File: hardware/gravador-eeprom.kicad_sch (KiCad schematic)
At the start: 21 parts, among them J1 Analog, J2 Digital, U1 74HC595, U2 74HC595, U4 28C256

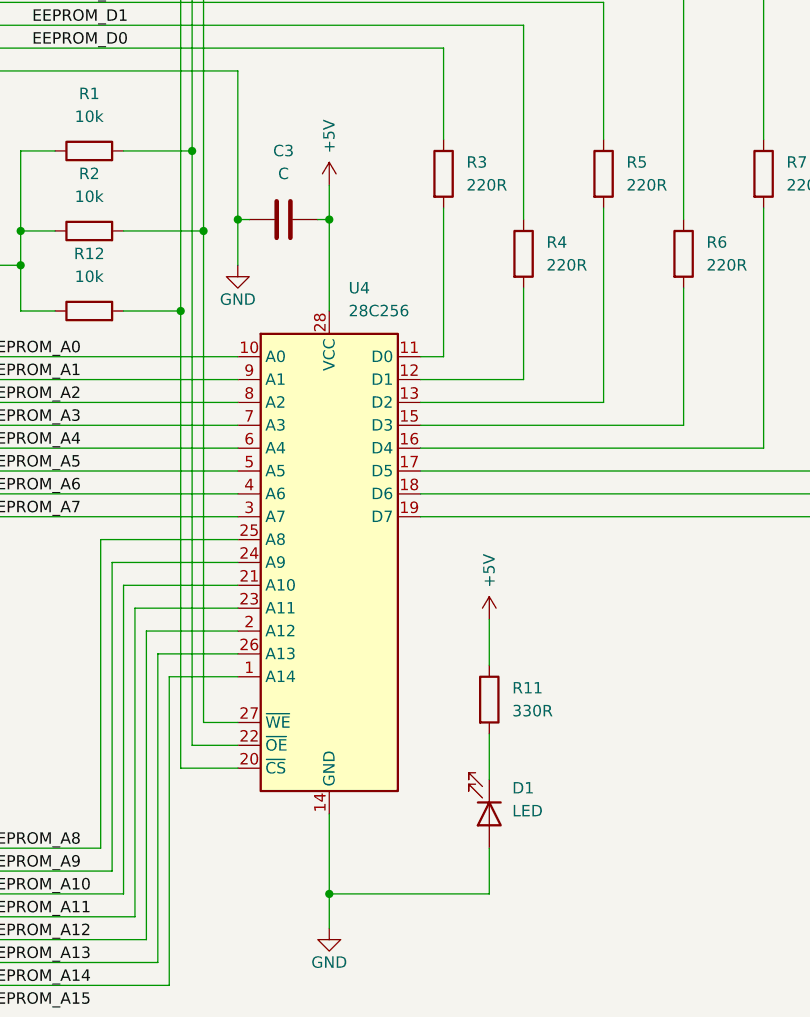
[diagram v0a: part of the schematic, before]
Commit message: Etapa 1: correções no esquema do hardware
- D1 (LED de alimentação) estava invertido: anodo no GND e catodo via
  R11 ao +5V, nunca acenderia. Símbolo girado 180°.
- C3 sem valor definido: agora 10uF (capacitor de reserva do soquete).
- PDF do esquema regenerado.

Co-Authored-By: Claude Opus 5.5 <noreply@anthropic.com>
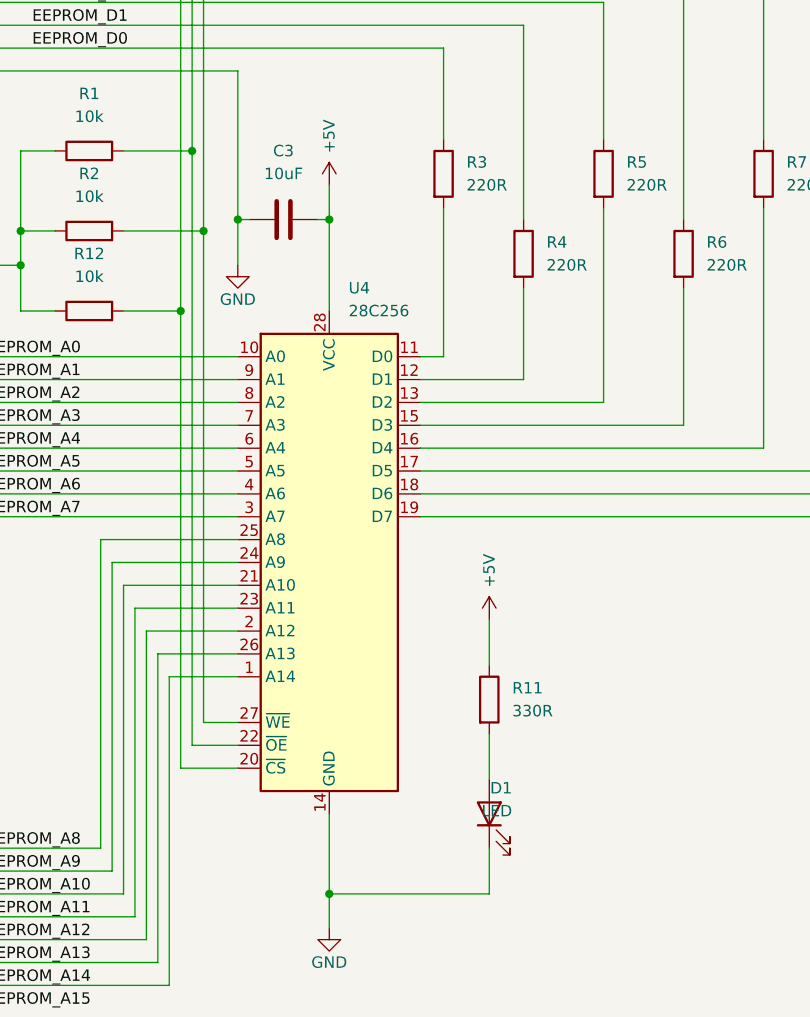
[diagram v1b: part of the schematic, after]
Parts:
- C3: value C -> 10uF
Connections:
- net GND: now also D1.1 (K); no longer D1.2 (A)
- net at R11.2: now also D1.2 (A); no longer D1.1 (K)
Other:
- moved on the sheet: D1
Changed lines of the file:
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@@
 	(symbol
 		(lib_id "Device:LED")
-		(at 162.56 137.16 270)
+		(at 162.56 137.16 90)
 		(unit 1)
 		(body_style 1)
@@
 			)
 		)
-		(property "Value" "C"
+		(property "Value" "10uF"
 			(at 139.7 66.04 90)
 			(show_name no)
